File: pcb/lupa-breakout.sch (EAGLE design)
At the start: 19 parts, among them J1 455-1750-1-ND

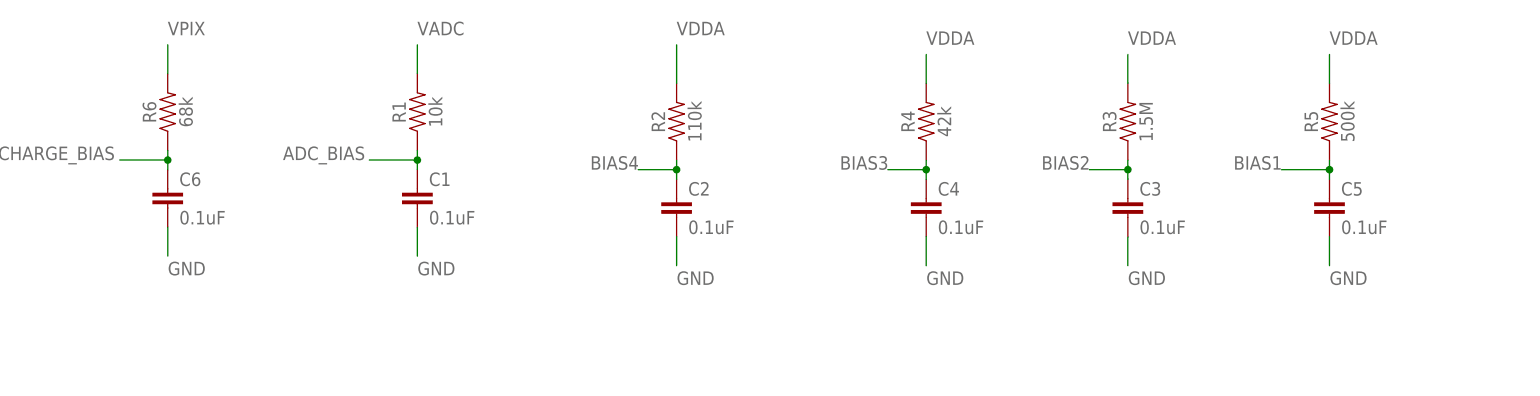
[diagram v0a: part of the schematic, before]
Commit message: made passices 1206 form factor
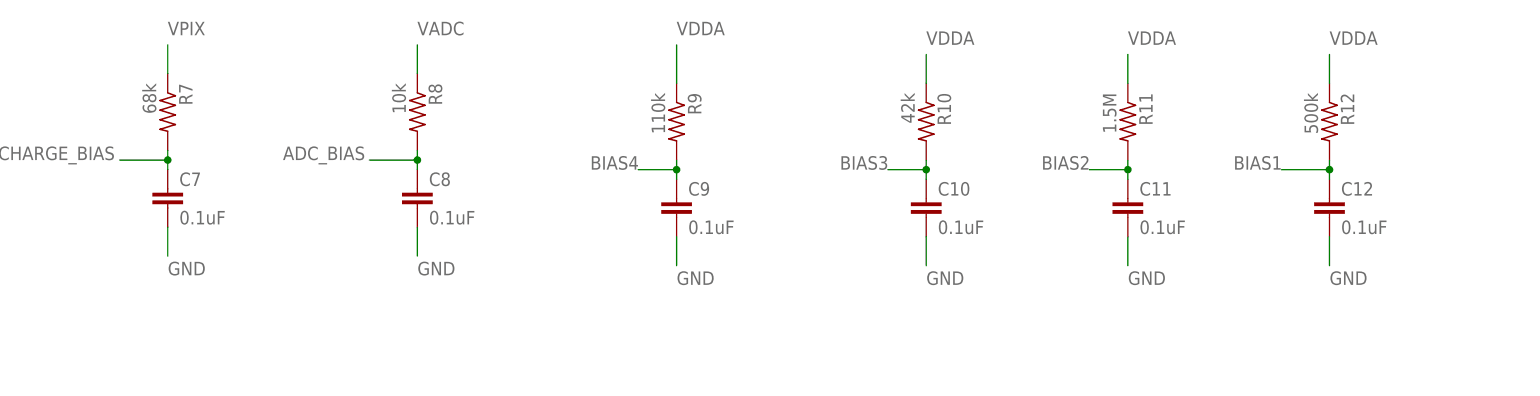
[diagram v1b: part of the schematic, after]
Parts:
- removed C1, C2, C3, C4, C5, C6: 0.1uF, SparkFun-Capacitors:0.1UF-0603-25V-(+80/-20%)
- removed R1: 10k, SparkFun-Resistors:10KOHM-0603-1/10W-1%
- removed R2: 110k, SparkFun-Resistors:10KOHM-0603-1/10W-1%
- removed R3: 1.5M, SparkFun-Resistors:10KOHM-0603-1/10W-1%
- removed R4: 42k, SparkFun-Resistors:10KOHM-0603-1/10W-1%
- removed R5: 500k, SparkFun-Resistors:10KOHM-0603-1/10W-1%
- removed R6: 68k, SparkFun-Resistors:10KOHM-0603-1/10W-1%
- added C10, C11, C12, C7, C8, C9: 0.1uF, rcl:C-EUC1206
- added R10: 42k, resistor:R-US_M1206
- added R11: 1.5M, resistor:R-US_M1206
- added R12: 500k, resistor:R-US_M1206
- added R7: 68k, resistor:R-US_M1206
- added R8: 10k, resistor:R-US_M1206
- added R9: 110k, resistor:R-US_M1206
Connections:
- net ADC_BIAS: now also C8.1, R8.2; no longer C1.1, R1.1
- net BIAS1: now also C12.1, R12.2; no longer C5.1, R5.1
- net BIAS2: now also C11.1, R11.2; no longer C3.1, R3.1
- net BIAS3: now also C10.1, R10.2; no longer C4.1, R4.1
- net BIAS4: now also C9.1, R9.2; no longer C2.1, R2.1
- net GND: now also C10.2, C11.2, C12.2, C7.2, C8.2, C9.2; no longer C1.2, C2.2, C3.2, C4.2, C5.2, C6.2
- net PRECHARGE_BIAS: now also C7.1, R7.2; no longer C6.1, R6.1
- net VADC: now also R8.1; no longer R1.2
- net VDDA: now also R10.1, R11.1, R12.1, R9.1; no longer R2.2, R3.2, R4.2, R5.2
- net VPIX: now also R7.1; no longer R6.2

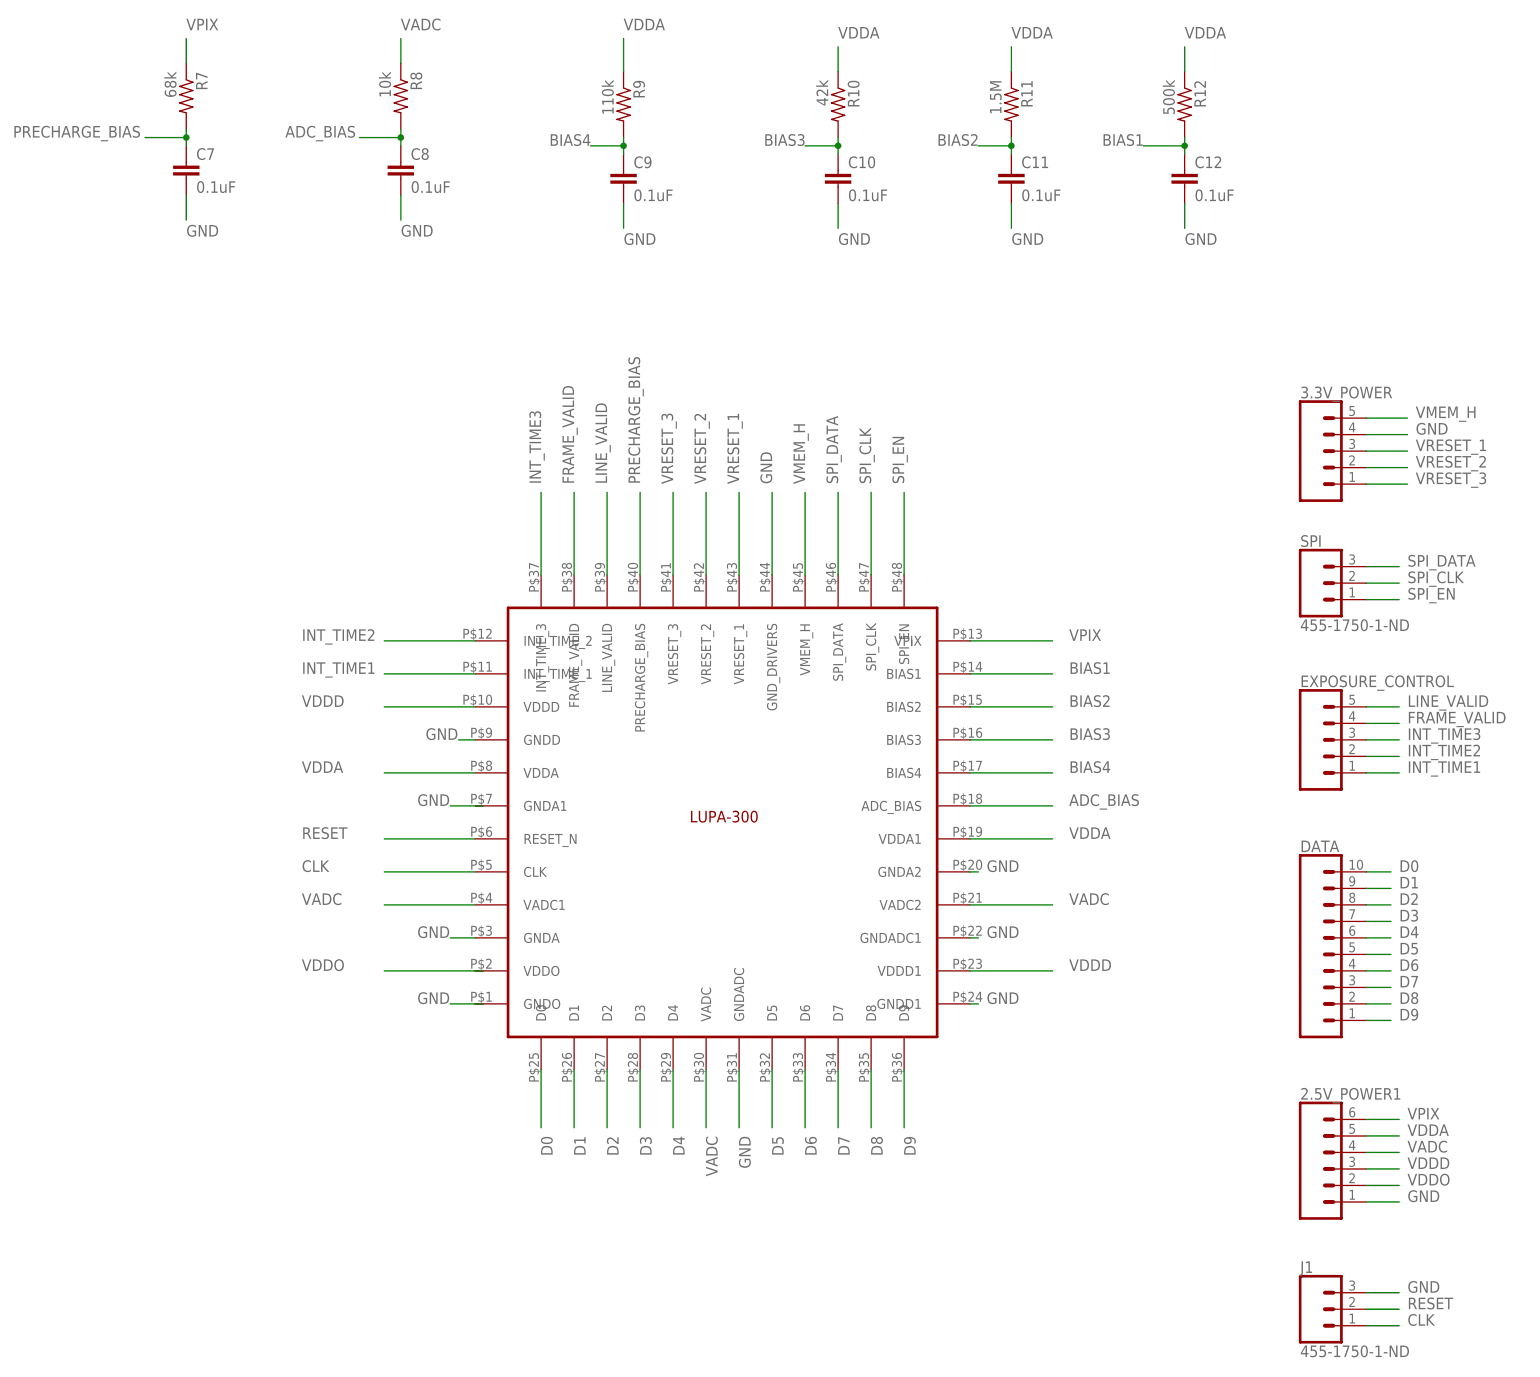
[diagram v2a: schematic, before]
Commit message: finalized breakout for lupa module
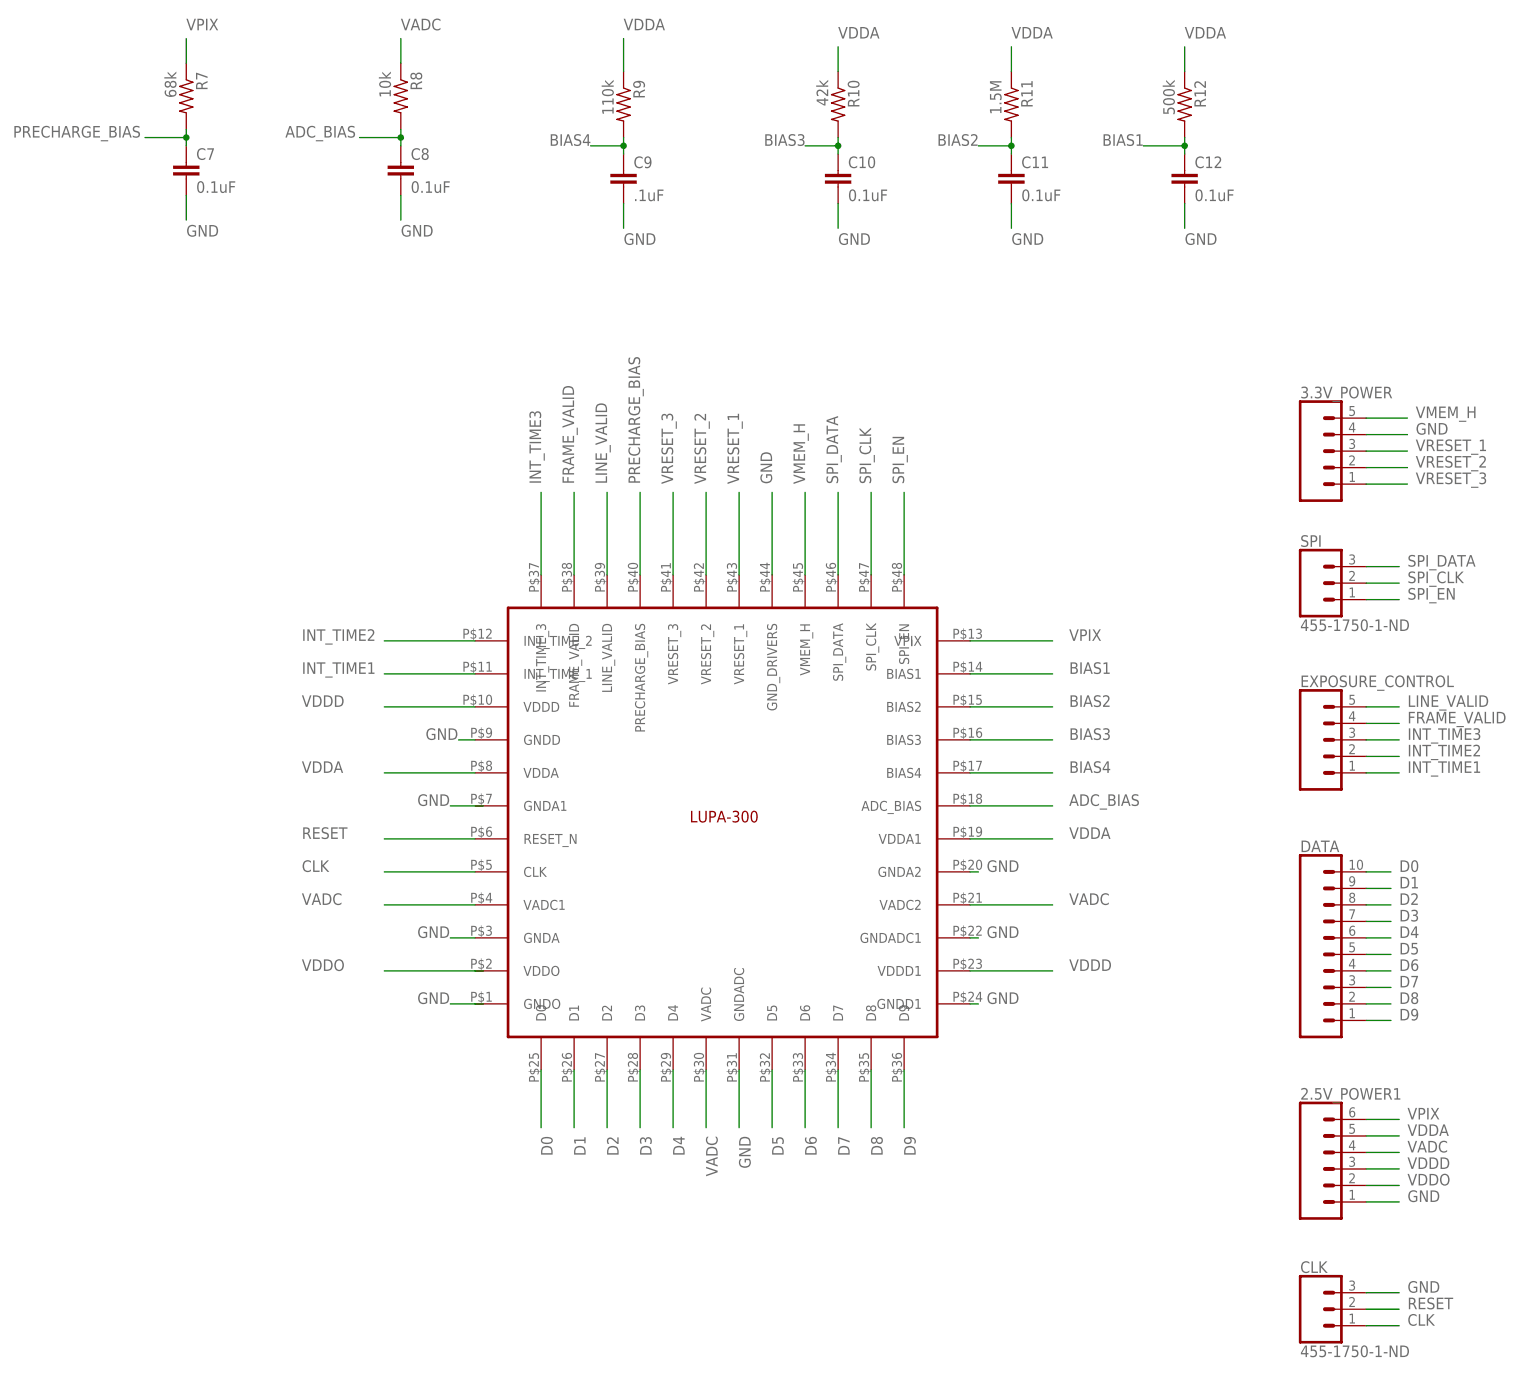
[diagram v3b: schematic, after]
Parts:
- C9: value 0.1uF -> .1uF
- renumbered J1 to CLK
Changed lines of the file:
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@@
 <part name="EXPOSURE_CONTROL" library="SparkFun-Connectors" deviceset="CONN_05" device=""/>
 <part name="2.5V_POWER1" library="SparkFun-Connectors" deviceset="CONN_06" device="SILK_FEMALE_PTH"/>
-<part name="J1" library="SparkFun-Connectors" deviceset="CONN_03" device="" value="455-1750-1-ND"/>
+<part name="CLK" library="SparkFun-Connectors" deviceset="CONN_03" device="" value="455-1750-1-ND"/>
 <part name="R7" library="resistor" library_urn="urn:adsk.eagle:library:348" deviceset="R-US_" device="M1206" package3d_urn="urn:adsk.eagle:package:26088/1" value="68k"/>
 <part name="R8" library="resistor" library_urn="urn:adsk.eagle:library:348" deviceset="R-US_" device="M1206" package3d_urn="urn:adsk.eagle:package:26088/1" value="10k"/>
@@
 <part name="C7" library="rcl" library_urn="urn:adsk.eagle:library:334" deviceset="C-EU" device="C1206" package3d_urn="urn:adsk.eagle:package:23618/2" value="0.1uF"/>
 <part name="C8" library="rcl" library_urn="urn:adsk.eagle:library:334" deviceset="C-EU" device="C1206" package3d_urn="urn:adsk.eagle:package:23618/2" value="0.1uF"/>
-<part name="C9" library="rcl" library_urn="urn:adsk.eagle:library:334" deviceset="C-EU" device="C1206" package3d_urn="urn:adsk.eagle:package:23618/2" value="0.1uF"/>
+<part name="C9" library="rcl" library_urn="urn:adsk.eagle:library:334" deviceset="C-EU" device="C1206" package3d_urn="urn:adsk.eagle:package:23618/2" value=".1uF"/>
 <part name="C10" library="rcl" library_urn="urn:adsk.eagle:library:334" deviceset="C-EU" device="C1206" package3d_urn="urn:adsk.eagle:package:23618/2" value="0.1uF"/>
 <part name="C11" library="rcl" library_urn="urn:adsk.eagle:library:334" deviceset="C-EU" device="C1206" package3d_urn="urn:adsk.eagle:package:23618/2" value="0.1uF"/>
@@
 <instance part="EXPOSURE_CONTROL" gate="G$1" x="180.34" y="74.93"/>
 <instance part="2.5V_POWER1" gate="G$1" x="182.88" y="8.89"/>
-<instance part="J1" gate="J$1" x="180.34" y="-12.7"/>
+<instance part="CLK" gate="J$1" x="180.34" y="-12.7"/>
 <instance part="R7" gate="G$1" x="6.35" y="173.99" rot="R270"/>
 <instance part="R8" gate="G$1" x="39.37" y="173.99" rot="R270"/>
@@
 </segment>
 <segment>
-<pinref part="J1" gate="J$1" pin="3"/>
+<pinref part="CLK" gate="J$1" pin="3"/>
 <wire x1="187.96" y1="-10.16" x2="193.04" y2="-10.16" width="0.1524" layer="91"/>
 <label x="194.31" y="-10.16" size="1.778" layer="95"/>
@@
 </segment>
 <segment>
-<pinref part="J1" gate="J$1" pin="1"/>
+<pinref part="CLK" gate="J$1" pin="1"/>
 <wire x1="187.96" y1="-15.24" x2="193.04" y2="-15.24" width="0.1524" layer="91"/>
 <label x="194.31" y="-15.24" size="1.778" layer="95"/>
@@
 </segment>
 <segment>
-<pinref part="J1" gate="J$1" pin="2"/>
+<pinref part="CLK" gate="J$1" pin="2"/>
 <wire x1="187.96" y1="-12.7" x2="193.04" y2="-12.7" width="0.1524" layer="91"/>
 <label x="194.31" y="-12.7" size="1.778" layer="95"/>
